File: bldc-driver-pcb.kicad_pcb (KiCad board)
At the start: 4 copper layers, 50 x 50 mm, 90 parts, among them IC1 ATSAMD21G18A-AFT, IC2 AS5047P-ATSM, IC3 L6498D, IC4 L6498D, IC5 L6498D, IC6 AD8030ARZ, IC7 AD8030ARZ, J1 FTSH-105-XX-X-DV, J2 505567-0471, J3 505567-0671, J4 505567-0671, J5 505567-0471, J7 USB3140-30-0170-1-C, Q1 IPD320N20N3GATMA1, Q2 IPD320N20N3GATMA1, Q3 IPD320N20N3GATMA1, Q4 IPD320N20N3GATMA1, Q5 IPD320N20N3GATMA1, Q6 IPD320N20N3GATMA1

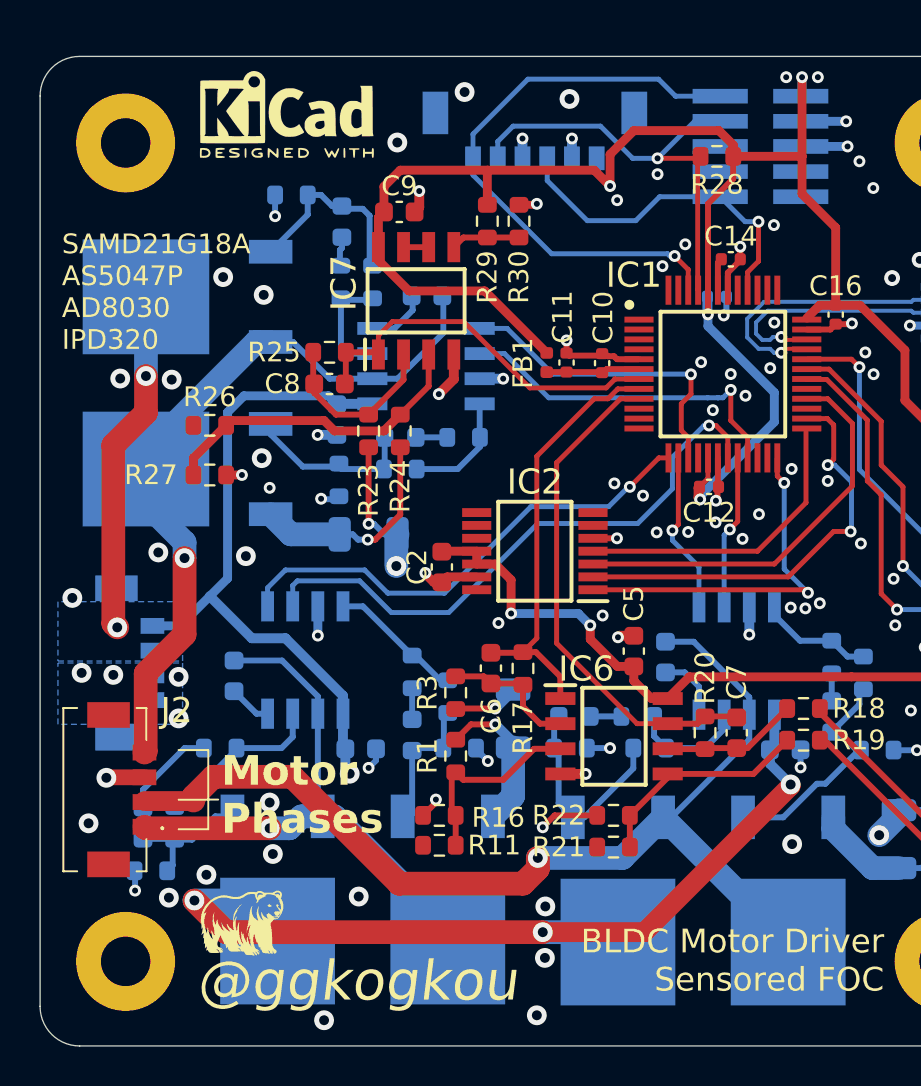
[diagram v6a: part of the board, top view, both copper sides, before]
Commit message: Relocate VM & phase connectors
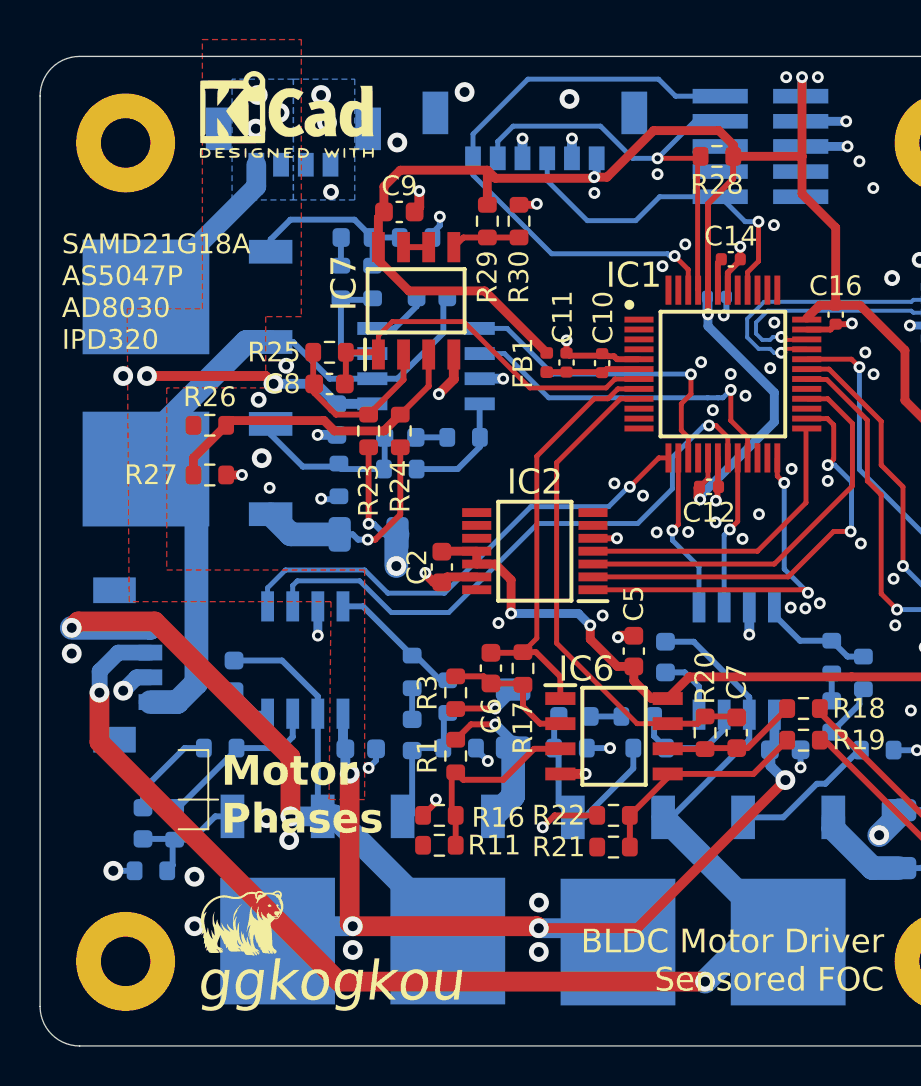
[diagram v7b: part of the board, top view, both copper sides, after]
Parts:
- J2: moved to B.Cu
- moved J5 28.1 mm to (127.8, 79.3), turned to 180 degrees
- moved R35 6.66 mm to (134.0, 84.6), turned to 0 degrees
- moved J2 6.31 mm to (119.0, 106.2), turned to -90 degrees
- moved D5 1.10 mm to (131.0, 84.6), turned to 0 degrees
- moved Cboot3 0.25 mm to (134.8, 87.6)
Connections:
- J5 pad 1: VBUS -> GND
- J5 pad 2: VBUS -> GND
- J5 pad 3: GND -> VBUS
- J5 pad 4: GND -> VBUS
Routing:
- net VBUS: track 98.4 -> 69.1 mm, vias 6 -> 9
- net /Three-Phase Inverter/HALF_BRIDGE_2_OUT: track 53.2 -> 69.6 mm, vias 1 -> 2
- net /Three-Phase Inverter/HALF_BRIDGE_1_OUT: track 29.7 -> 43.0 mm, vias 1 -> 2
- net +3V3: track 138.4 -> 136.4 mm
- net /Three-Phase Inverter/HALF_BRIDGE_3_OUT: track 37.8 -> 36.7 mm, vias 1 -> 0
- net GND: track 79.9 -> 79.8 mm, vias 110 -> 102
- added copper zone on F.Cu, net VBUS
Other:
- board text added: "ggkogkou"
- board text removed: "@ggkogkou"

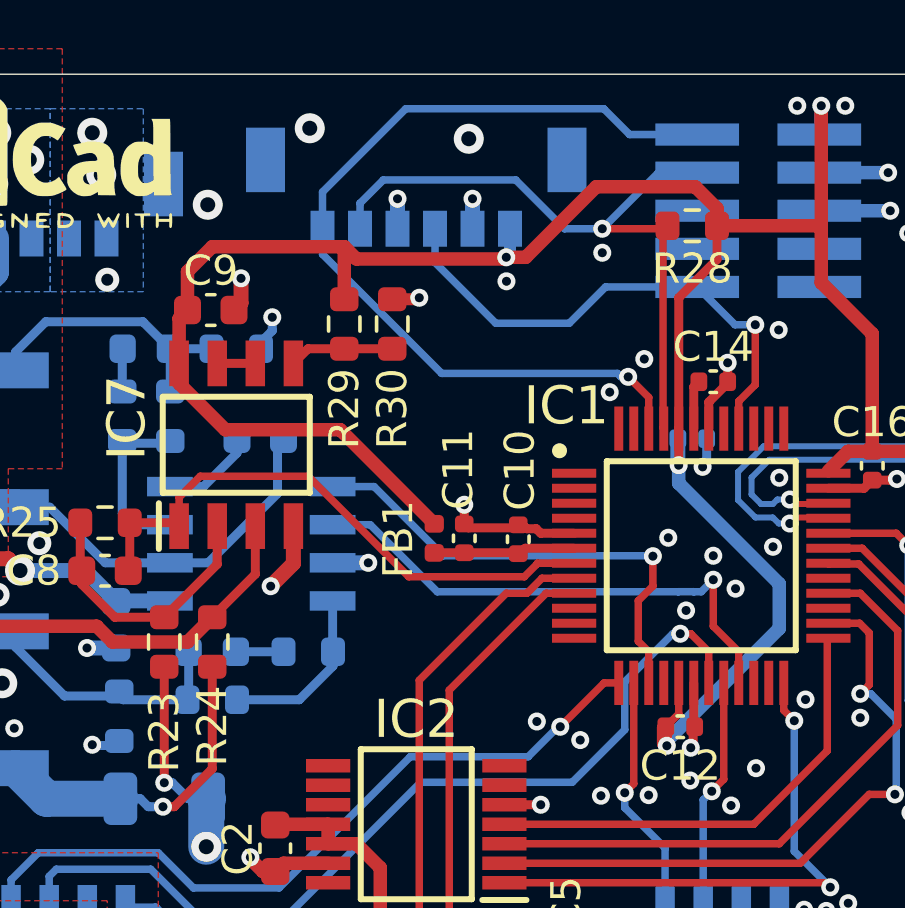
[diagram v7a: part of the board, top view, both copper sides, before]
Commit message: Add 32.768kHz external clock & specify ferrite bead part number
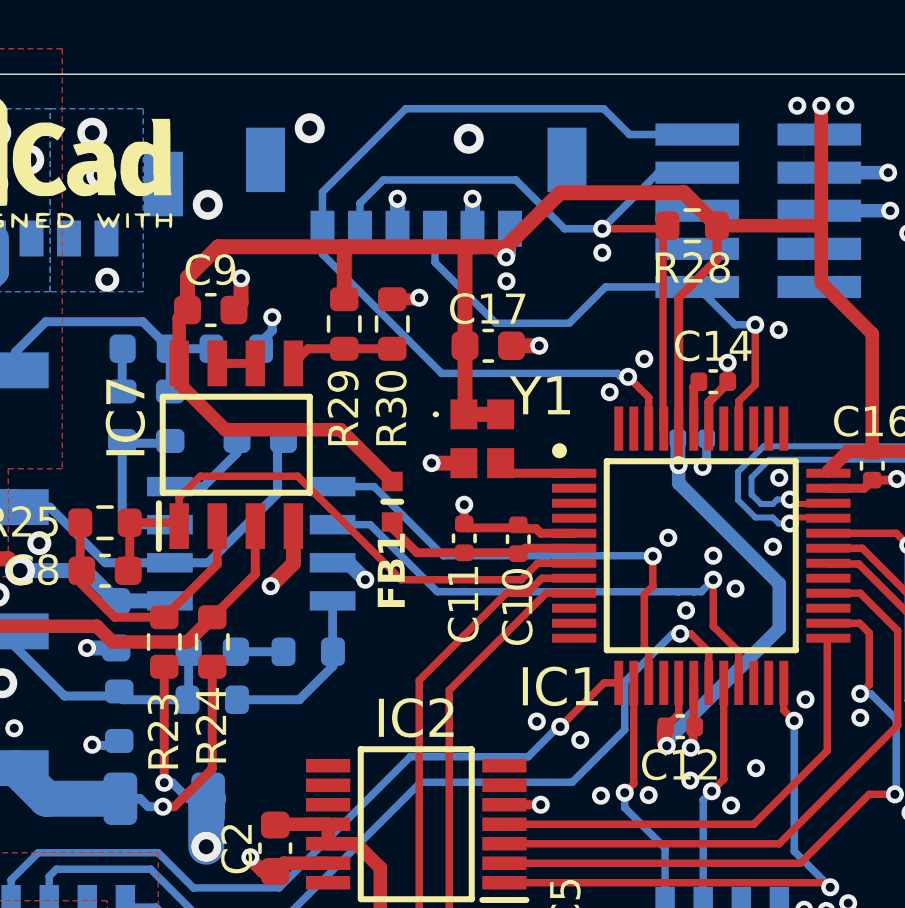
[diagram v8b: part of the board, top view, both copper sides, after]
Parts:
- added C17: 0.1u, Capacitor_SMD:C_0603_1608Metric, F.Cu at (142.4, 84.5)
- added Y1: LFSPXO009686, bldc-driver-pcb:LFSPXO009686, F.Cu at (142.2, 87.6)
- FB1: footprint Inductor_SMD:L_0402_1005Metric -> bldc-driver-pcb:BLM18SP221SN1B
- moved FB1 1.86 mm to (139.2, 89.7)
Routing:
- net +3V3: track 136.4 -> 141.2 mm
- net /Microcontroller/XIN32: track 0.00 -> 2.59 mm
- net GND: track 79.8 -> 82.0 mm, vias 102 -> 104
- net /Microcontroller/VDDANA: track 4.75 -> 6.69 mm
